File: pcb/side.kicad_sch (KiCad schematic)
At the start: 61 parts, among them SW1 SW_Push, SW10 SW_Push, SW13 SW_Push, SW14 SW_Push, SW15 SW_Push, SW16 SW_Push, SW17 SW_Push, SW18 SW_Push, SW25 SW_Push, SW26 SW_Push, SW27 SW_Push, SW28 SW_Push, SW29 SW_Push, SW3 SW_Push, SW30 SW_Push, SW31 SW_Push, SW32 SW_Push, SW33 SW_Push, SW34 SW_Push, SW35 SW_Push, SW36 SW_Push, SW49 SW_Push, SW5 SW_Push, SW6 SW_Push, SW9 SW_Push, U1 XIAO-nRF52840-SMD

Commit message: Add BMS and LEDs
Added a Battery Management system and some RGB LED backlight
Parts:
- removed H13: MountingHole, MountingHole:MountingHole_3.2mm_M3, symbol Mechanical:MountingHole
- added C1: 0.1u, symbol Device:C
- added C11, C13, C15, C17, C19, C21, C22, C23, C24, C25, C26, C33, C34, C35, C36, C37, C38, C45, C46, C47, C48, C49, C50, C60, C61, C62, C9: 100n, symbol Device:C
- added C3: 10u, symbol Device:C
- added C5, C7: 22u, symbol Device:C
- added C57: 470u, symbol Device:C_Polarized
- added D51, D53: D, Diode_SMD:D_SOD-123, symbol Device:D
- added D55: SS34, Diode_SMD:D_SMA, symbol Diode:SS34
- added L1: PNLS8040-100M 10UH, symbol Device:L
- added LED1, LED11, LED13, LED14, LED15, LED16, LED17, LED18, LED25, LED26, LED27, LED28, LED29, LED3, LED30, LED37, LED38, LED39, LED40, LED41, LED42, LED5, LED52, LED53, LED54, LED7, LED9: choc_SK6812MINI-E, PCM_marbastlib-choc:LED_choc_6028R, symbol PCM_marbastlib-choc:choc_SK6812MINI-E
- added R11: 73k2, symbol Device:R
- added R13: 220R, symbol Device:R
- added R5: 470R, symbol Device:R
- added R7: 2k, symbol Device:R
- added R9: 10k, symbol Device:R
- added SW51: SW_Push, marbastlib-choc:SW_choc_v1_HS_CPG135001S30_1.5u, symbol Switch:SW_Push
- added SW53: SW_Push, PCM_marbastlib-choc:SW_choc_v1_HS_CPG135001S30_1u, symbol Switch:SW_Push
- added U3: DW01A, Package_TO_SOT_SMD:SOT-23-6, symbol Battery_Management:DW01A
- added U5: FS8205, Package_TO_SOT_SMD:SOT-23-6, symbol PCM_marbastlib-various:FS8205
- added U7: MT3608, Package_TO_SOT_SMD:SOT-23-6, symbol Regulator_Switching:MT3608
- SW49: footprint PCM_marbastlib-choc:SW_choc_v1_HS_CPG135001S30_1u -> marbastlib-choc:SW_choc_v1_HS_CPG135001S30_1.75u
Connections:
- net COL1: now also SW27.1
- net COL3: now also SW53.1
- net COL4: now also SW51.1
- net GND: now also C11.1, C13.1, C15.1, C17.1, C19.1, C21.1, C22.1, C23.1, C24.1, C25.1, C26.1, C3.2, C33.1, C34.1, C35.1, C36.1, C37.1, C38.1, C45.1, C46.1, C47.1, C48.1, C49.1, C5.2, C50.1, C57.2, C60.1, C61.1, C62.1, C7.2, C9.1, LED1.4 (VSS), LED11.4 (VSS), LED13.4 (VSS), LED14.4 (VSS), LED15.4 (VSS), LED16.4 (VSS), LED17.4 (VSS), LED18.4 (VSS), LED25.4 (VSS), LED26.4 (VSS), LED27.4 (VSS), LED28.4 (VSS), LED29.4 (VSS), LED3.4 (VSS), LED30.4 (VSS), LED37.4 (VSS), LED38.4 (VSS), LED39.4 (VSS), LED40.4 (VSS), LED41.4 (VSS), LED42.4 (VSS), LED5.4 (VSS), LED52.4 (VSS), LED53.4 (VSS), LED54.4 (VSS), LED7.4 (VSS), LED9.4 (VSS), R7.1, R9.2, U5.3 (S2), U7.2 (GND); no longer TP3.1
- net ROW4: now also D51.1 (K), D53.1 (K)
- net VBAT: no longer TP1.1
- new net: LED38.2 (DOUT), LED39.3 (DIN)
- new net: LED37.2 (DOUT), LED38.3 (DIN)
- new net: C1.1, R5.2, U3.5 (VCC)
- new net: LED1.3 (DIN), R13.2
- new net: LED11.3 (DIN), LED9.2 (DOUT)
- new net: LED7.2 (DOUT), LED9.3 (DIN)
- new net: D55.2 (A), L1.2, U7.1 (SW)
- new net: R11.2, R9.1, U7.3 (FB)
- new net: LED29.2 (DOUT), LED30.3 (DIN)
- new net: LED28.2 (DOUT), LED29.3 (DIN)
- new net: LED53.2 (DOUT), LED54.3 (DIN)
- new net: LED52.2 (DOUT), LED53.3 (DIN)
- new net: LED5.2 (DOUT), LED7.3 (DIN)
- new net: LED42.2 (DOUT), LED52.3 (DIN)
- new net: LED13.2 (DOUT), LED14.3 (DIN)
- new net: LED11.2 (DOUT), LED13.3 (DIN)
- new net: R7.2, U3.2 (CS)
- new net: LED26.2 (DOUT), LED27.3 (DIN)
- new net: LED25.2 (DOUT), LED26.3 (DIN)
- new net: U3.3 (OC), U5.4 (G2)
- new net: U3.1 (OD), U5.6 (G1)
- new net: D53.2 (A), SW53.2
- new net: LED30.2 (DOUT), LED37.3 (DIN)
- new net: D51.2 (A), SW51.2
- new net: LED18.2 (DOUT), LED25.3 (DIN)
- new net: LED17.2 (DOUT), LED18.3 (DIN)
- new net: LED41.2 (DOUT), LED42.3 (DIN)
- new net: LED40.2 (DOUT), LED41.3 (DIN)
- new net: LED15.2 (DOUT), LED16.3 (DIN)
- new net: LED14.2 (DOUT), LED15.3 (DIN)
- new net: LED39.2 (DOUT), LED40.3 (DIN)
- new net: LED16.2 (DOUT), LED17.3 (DIN)
- new net: LED3.2 (DOUT), LED5.3 (DIN)
- new net: LED1.2 (DOUT), LED3.3 (DIN)
- new net: LED27.2 (DOUT), LED28.3 (DIN)
- new net +5V: C11.2, C13.2, C15.2, C17.2, C19.2, C21.2, C22.2, C23.2, C24.2, C25.2, C26.2, C33.2, C34.2, C35.2, C36.2, C37.2, C38.2, C45.2, C46.2, C47.2, C48.2, C49.2, C50.2, C57.1, C60.2, C61.2, C62.2, C7.1, C9.2, D55.1 (K), LED1.1 (VDD), LED11.1 (VDD), LED13.1 (VDD), LED14.1 (VDD), LED15.1 (VDD), LED16.1 (VDD), LED17.1 (VDD), LED18.1 (VDD), LED25.1 (VDD), LED26.1 (VDD), LED27.1 (VDD), LED28.1 (VDD), LED29.1 (VDD), LED3.1 (VDD), LED30.1 (VDD), LED37.1 (VDD), LED38.1 (VDD), LED39.1 (VDD), LED40.1 (VDD), LED41.1 (VDD), LED42.1 (VDD), LED5.1 (VDD), LED52.1 (VDD), LED53.1 (VDD), LED54.1 (VDD), LED7.1 (VDD), LED9.1 (VDD), R11.1
- new net +BATT: C3.1, C5.1, L1.1, R5.1, TP1.1, U7.4 (EN), U7.5 (IN)
- new net -BATT: C1.2, TP3.1, U3.6 (GND), U5.1 (S1)
- new net LED_DIN: R13.1
- no-connect marks 8 -> 10
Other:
- note added: "5V BUCK CONVERTER"
- note added: "BATTERY PROTECTION"
- note added: "MOUNTING HOLES"
- note added: "RGB BACKLIGHT"
- note removed: "MOUNTING POINTS"
- moved on the sheet: H11, H3, H5, H7, H9

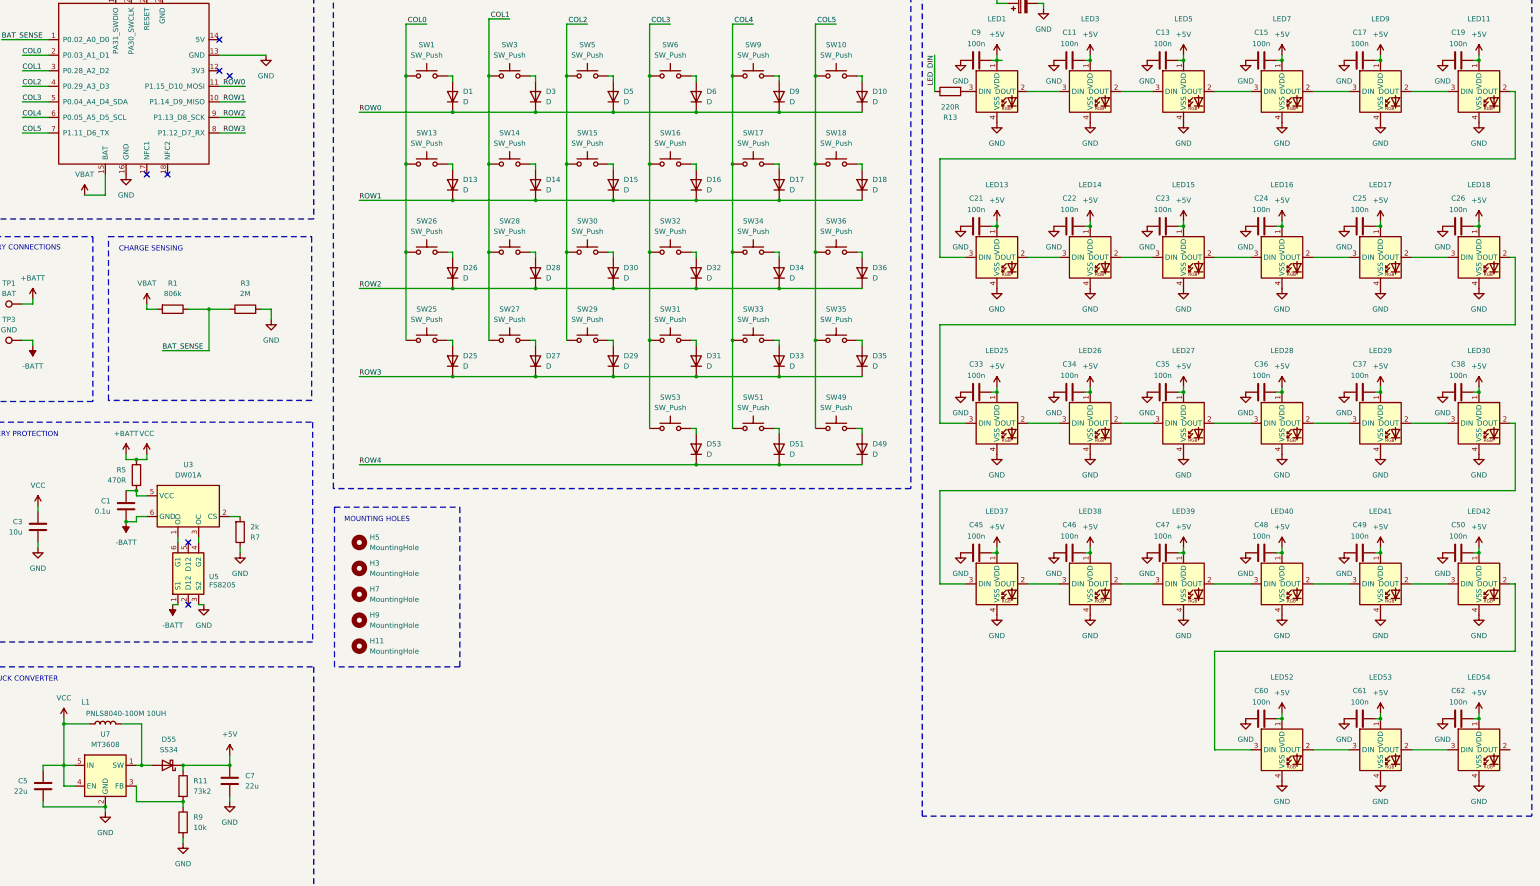
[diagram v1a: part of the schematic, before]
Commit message: Add other half
Designed, Placed and Routed the other half of the PCB
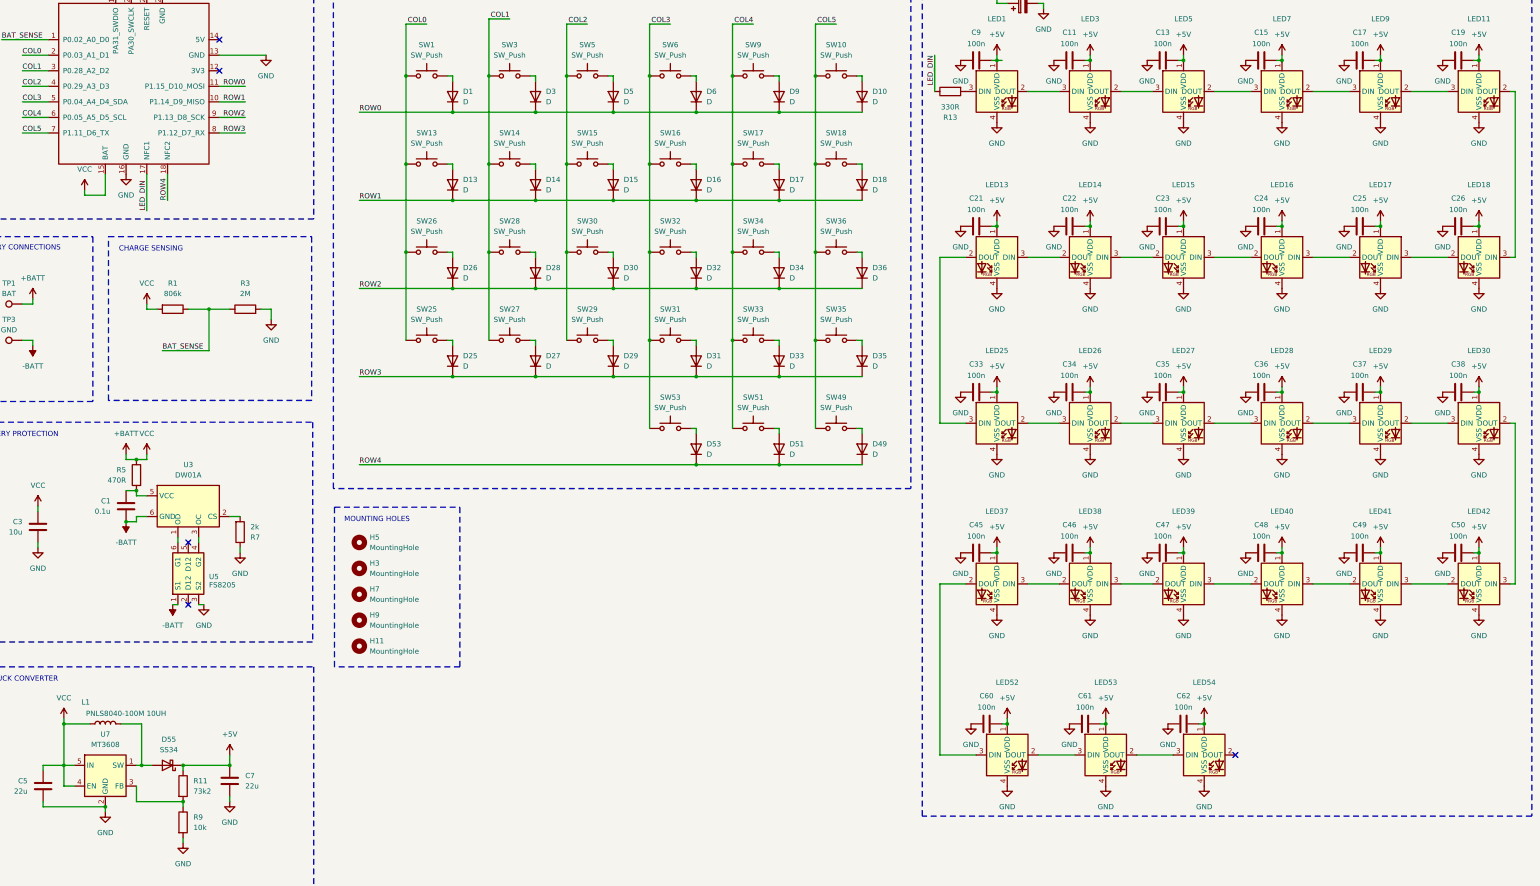
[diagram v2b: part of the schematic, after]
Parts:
- C1, C11, C13, C15, C17, C19, C21, C22, C23, C24, C25, C26, C3, C33, C34, C35, C36, C37, C38, C45, C46, C47, C48, C49, C5, C50, C60, C61, C62, C7, C9: footprint (none) -> Capacitor_SMD:C_0805_2012Metric_Pad1.18x1.45mm_HandSolder
- C57: footprint (none) -> Capacitor_SMD:CP_Elec_6.3x7.7
- L1: footprint (none) -> Inductor_SMD:L_Cenker_CKCS8040
- LED13, LED14, LED15, LED16, LED17, LED18, LED37, LED38, LED39, LED40, LED41, LED42: footprint PCM_marbastlib-choc:LED_choc_6028R -> PCM_marbastlib-choc:LED_choc_6028R-ROT
- R1, R3: footprint Resistor_SMD:R_0805_2012Metric -> Resistor_SMD:R_0805_2012Metric_Pad1.20x1.40mm_HandSolder
- R11, R5, R7, R9: footprint (none) -> Resistor_SMD:R_0805_2012Metric_Pad1.20x1.40mm_HandSolder
- R13: value 220R -> 330R; footprint (none) -> Resistor_SMD:R_0805_2012Metric_Pad1.20x1.40mm_HandSolder
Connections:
- net VBAT is gone; now on net +BATT: R1.2, U1.15 (BAT)
- net LED_DIN: now also U1.17 (NFC1)
- net ROW4: now also U1.18 (NFC2)
- net at LED38.2 (DOUT): now also LED37.3 (DIN); no longer LED39.3 (DIN)
- net at LED38.3 (DIN): now also LED39.2 (DOUT); no longer LED37.2 (DOUT)
- net at LED52.3 (DIN): now also LED37.2 (DOUT); no longer LED42.2 (DOUT)
- net at LED13.2 (DOUT): now also LED25.3 (DIN); no longer LED14.3 (DIN)
- net at LED13.3 (DIN): now also LED14.2 (DOUT); no longer LED11.2 (DOUT)
- net at LED30.2 (DOUT): now also LED42.3 (DIN); no longer LED37.3 (DIN)
- net at LED18.2 (DOUT): now also LED17.3 (DIN); no longer LED25.3 (DIN)
- net at LED18.3 (DIN): now also LED11.2 (DOUT); no longer LED17.2 (DOUT)
- net at LED41.2 (DOUT): now also LED40.3 (DIN); no longer LED42.3 (DIN)
- net at LED41.3 (DIN): now also LED42.2 (DOUT); no longer LED40.2 (DOUT)
- net at LED15.2 (DOUT): now also LED14.3 (DIN); no longer LED16.3 (DIN)
- net at LED15.3 (DIN): now also LED16.2 (DOUT); no longer LED14.2 (DOUT)
- new net: LED39.3 (DIN), LED40.2 (DOUT)
- new net: LED16.3 (DIN), LED17.2 (DOUT)
- no-connect marks 10 -> 8
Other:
- moved on the sheet: C60, C61, C62, LED52, LED53, LED54

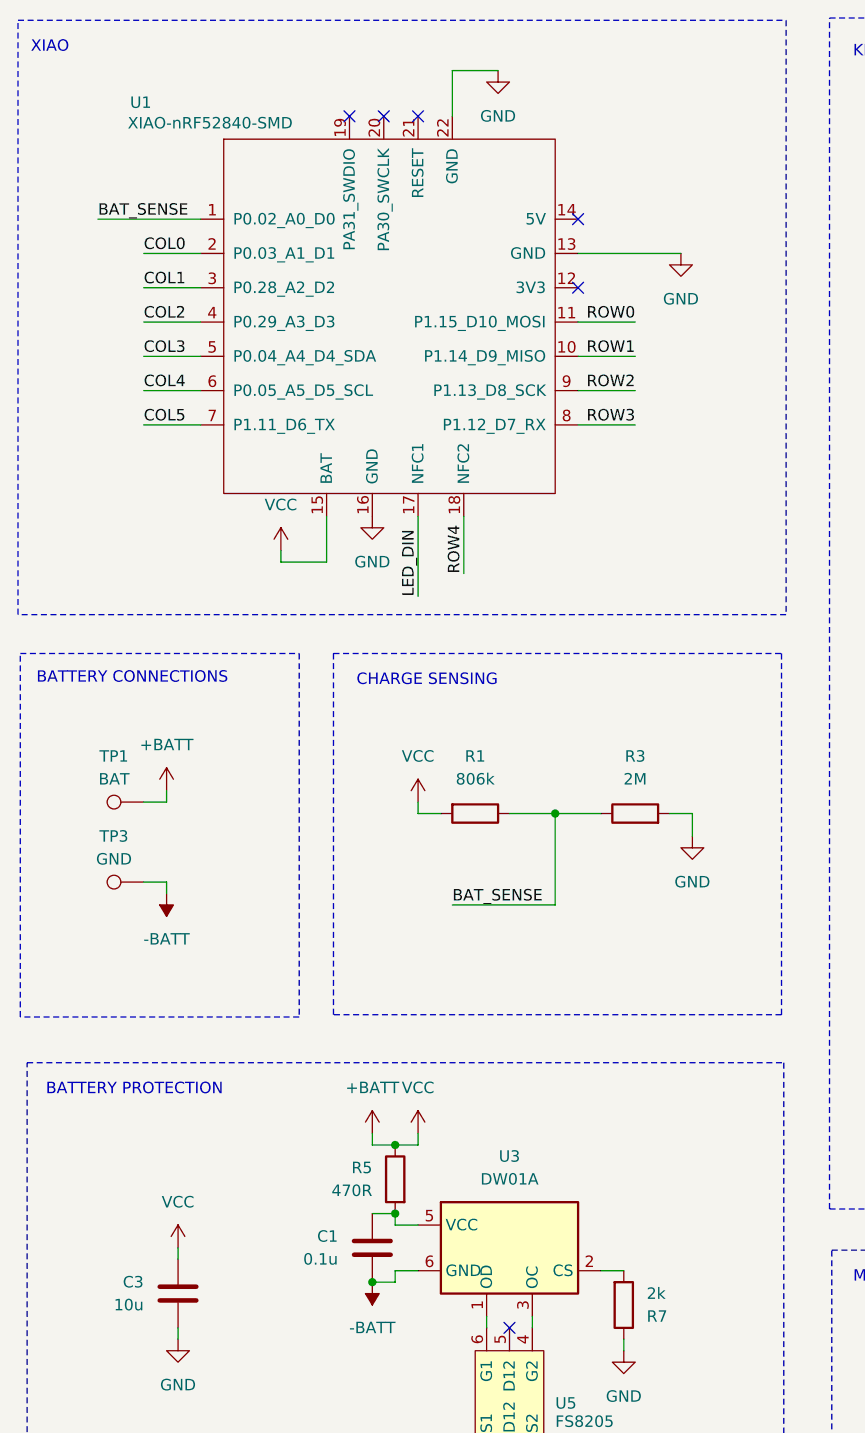
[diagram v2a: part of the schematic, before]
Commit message: Finished Designing PCB
Finished Desiging the PCB and exported gerbers for manufacturing
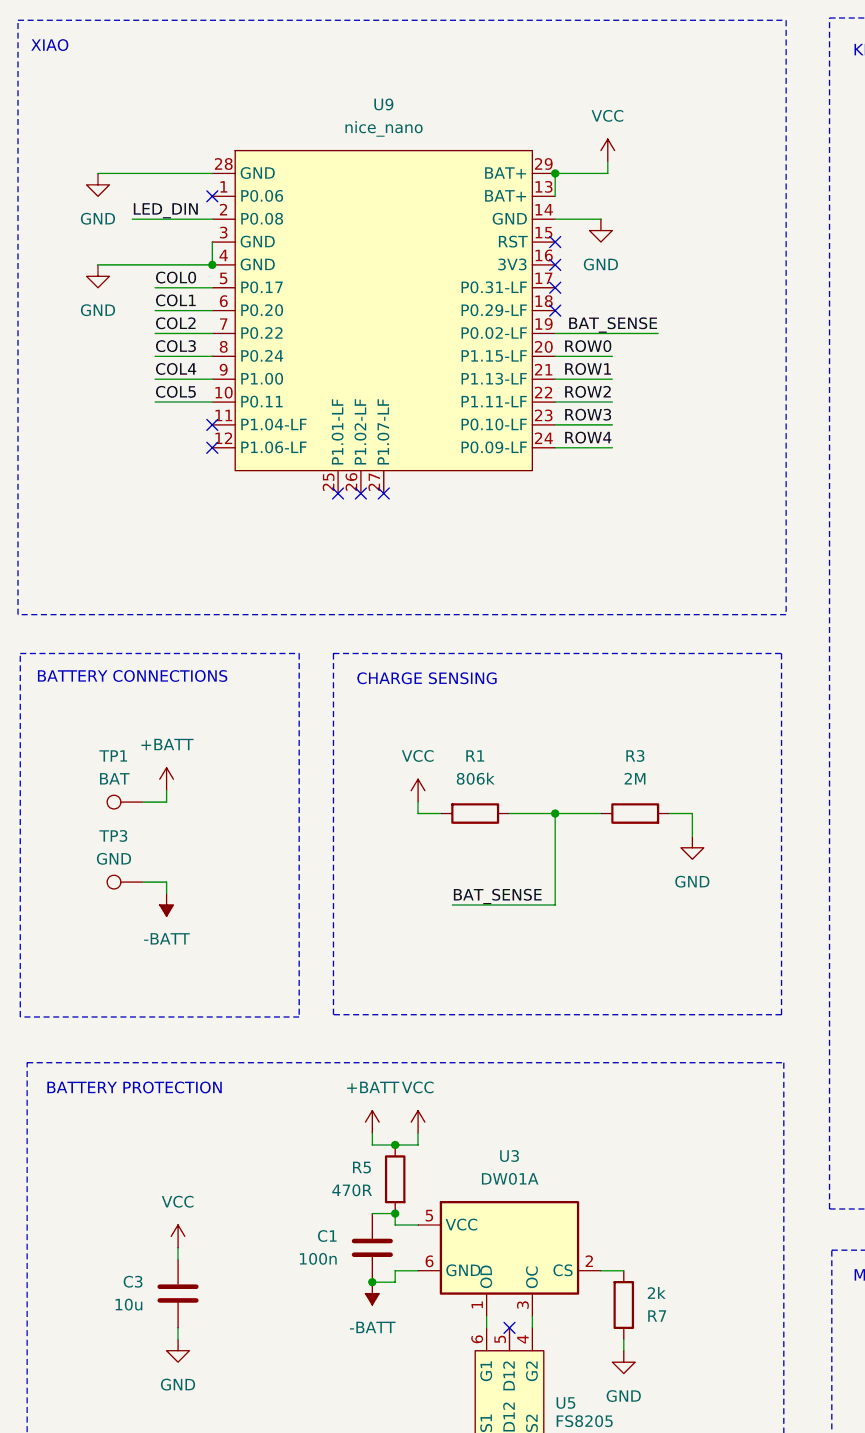
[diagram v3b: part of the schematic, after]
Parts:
- removed U1: XIAO-nRF52840-SMD, pcb:modified-XIAO-nRF52840-SMD, symbol Seeed_Studio_XIAO_Series:XIAO-nRF52840-SMD
- added U9: nice_nano, PCM_marbastlib-xp-promicroish:nice_nano_AH_USBup, symbol PCM_marbastlib-promicroish:nice_nano
- C1: value 0.1u -> 100n
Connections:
- net +BATT: now also U9.13 (BAT+), U9.29 (BAT+)
- net BAT_SENSE: now also U9.19 (P0.02-LF)
- net COL0: now also U9.5 (P0.17)
- net COL1: now also U9.6 (P0.20)
- net COL2: now also U9.7 (P0.22)
- net COL3: now also U9.8 (P0.24)
- net COL4: now also U9.9 (P1.00)
- net COL5: now also U9.10 (P0.11)
- net GND: now also U9.14 (GND), U9.28 (GND), U9.3 (GND), U9.4 (GND)
- net LED_DIN: now also U9.2 (P0.08)
- net ROW0: now also U9.20 (P1.15-LF)
- net ROW1: now also U9.21 (P1.13-LF)
- net ROW2: now also U9.22 (P1.11-LF)
- net ROW3: now also U9.23 (P0.10-LF)
- net ROW4: now also U9.24 (P0.09-LF)
- no-connect marks 8 -> 13
